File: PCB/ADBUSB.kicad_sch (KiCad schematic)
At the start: 6 parts, among them J1 MLD-MDC-4-02, J2 MLD-MDC-4-02, SW1 SW_SPST, U1 ProMicro

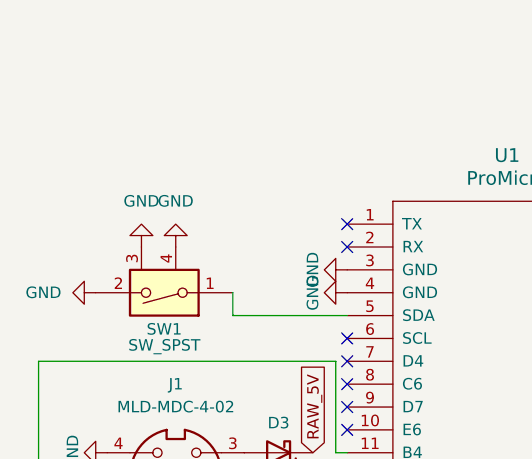
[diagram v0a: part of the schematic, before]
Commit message: Add a second button footprint
So one can either use an horizontal or vertical one
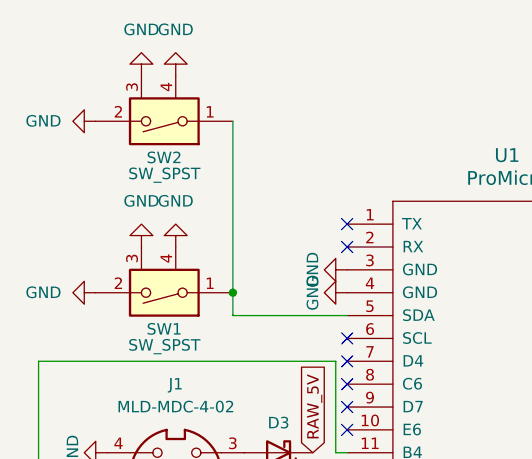
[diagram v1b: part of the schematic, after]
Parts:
- added SW2: SW_SPST, Pushbutton:SPST_power_switch, symbol Switch:SW_DIP_x01
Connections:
- net GND: now also SW2.2, SW2.3, SW2.4 (3)
- net at SW1.1, U1.5 (SDA): now also SW2.1
